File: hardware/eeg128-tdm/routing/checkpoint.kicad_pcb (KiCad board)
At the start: 4 copper layers, 190 x 110 mm, 642 parts, among them J1 J1, J10 J10, J11 J11, J2 J2, J3 J3, J4 J4, J5 J5, J6 J6, J7 J7, J8 J8, J9 TYPE-C-31-M-12, U1 U1, U10 U10, U11 U11, U12 U12, U13 U13, U14 U14, U15 U15, U16 U16, U17 U17, U18 U18, U19 U19, U2 U2, U20 U20, U21 U21, U22 U22, U23 U23, U24 U24, U25 U25, U26 U26, U27 U27, U3 U3, U4 U4, U5 U5, U6 U6, U7 U7, U8 U8, U9 U9, Y1 Y1

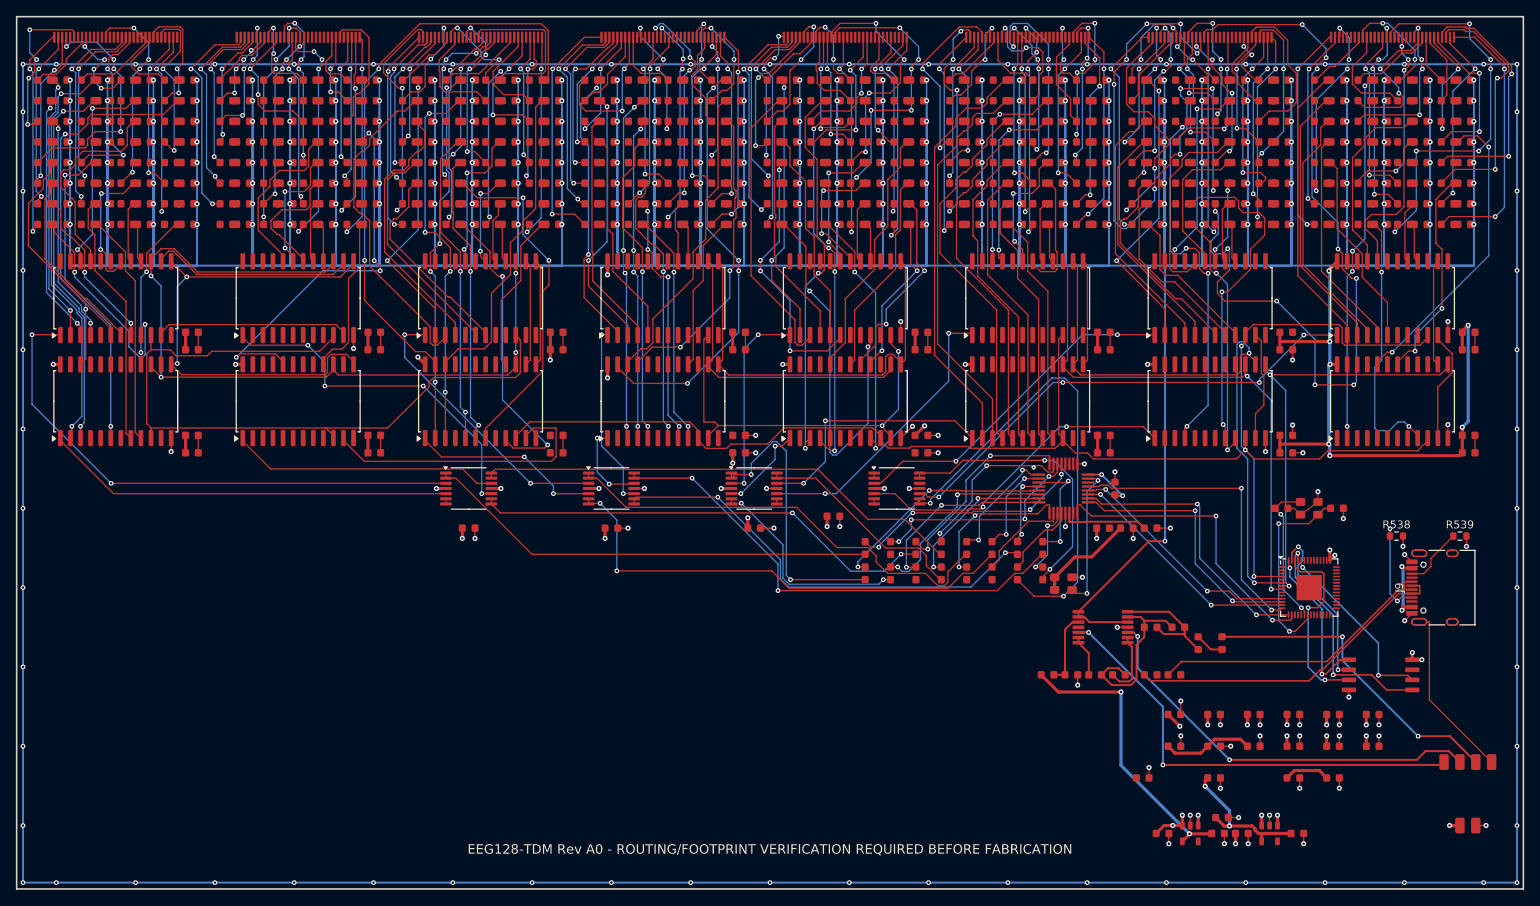
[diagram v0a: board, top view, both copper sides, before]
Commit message: Continue A2 at 316 opens and guard sensitive analog layer routing
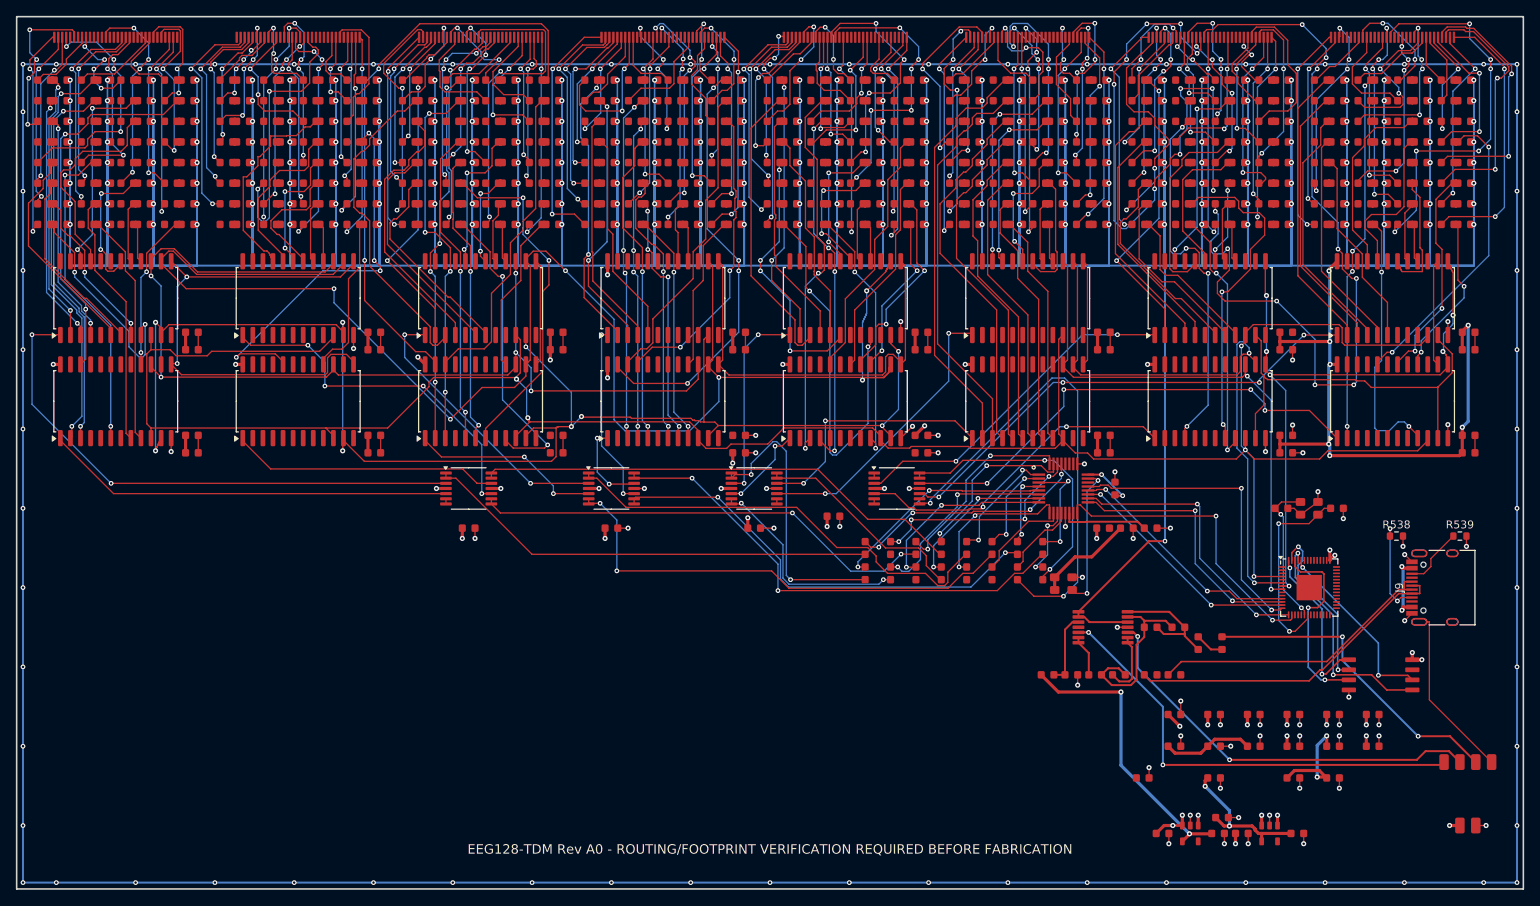
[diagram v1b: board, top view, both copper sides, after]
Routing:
- net MUX_S2: track 168.6 -> 295.6 mm, vias 2 -> 8
- net MUX_S1: track 140.3 -> 235.9 mm, vias 2 -> 9
- net BANK7_N_MUX_OUT: track 0.00 -> 61.8 mm, vias 0 -> 4
- net CH018_N_ELECTRODE: track 0.00 -> 34.9 mm, vias 0 -> 2
- net MUX_EN: track 171.4 -> 200.6 mm, vias 6 -> 7
- net MUX_S3: track 197.1 -> 224.3 mm, vias 4 -> 8
- net CH026_P_MUX: track 0.50 -> 26.4 mm
- net CH127_N_MUX: track 0.50 -> 20.9 mm, vias 0 -> 2
- net CH125_P_MUX: track 0.50 -> 16.4 mm
- net CH054_N_ELECTRODE: track 0.00 -> 13.3 mm
- net 3V3D: track 53.9 -> 60.9 mm, vias 15 -> 16
- net MUX_S0: track 295.6 -> 302.0 mm, vias 3 -> 5

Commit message: Resume validated A2 routing from 313 native opens
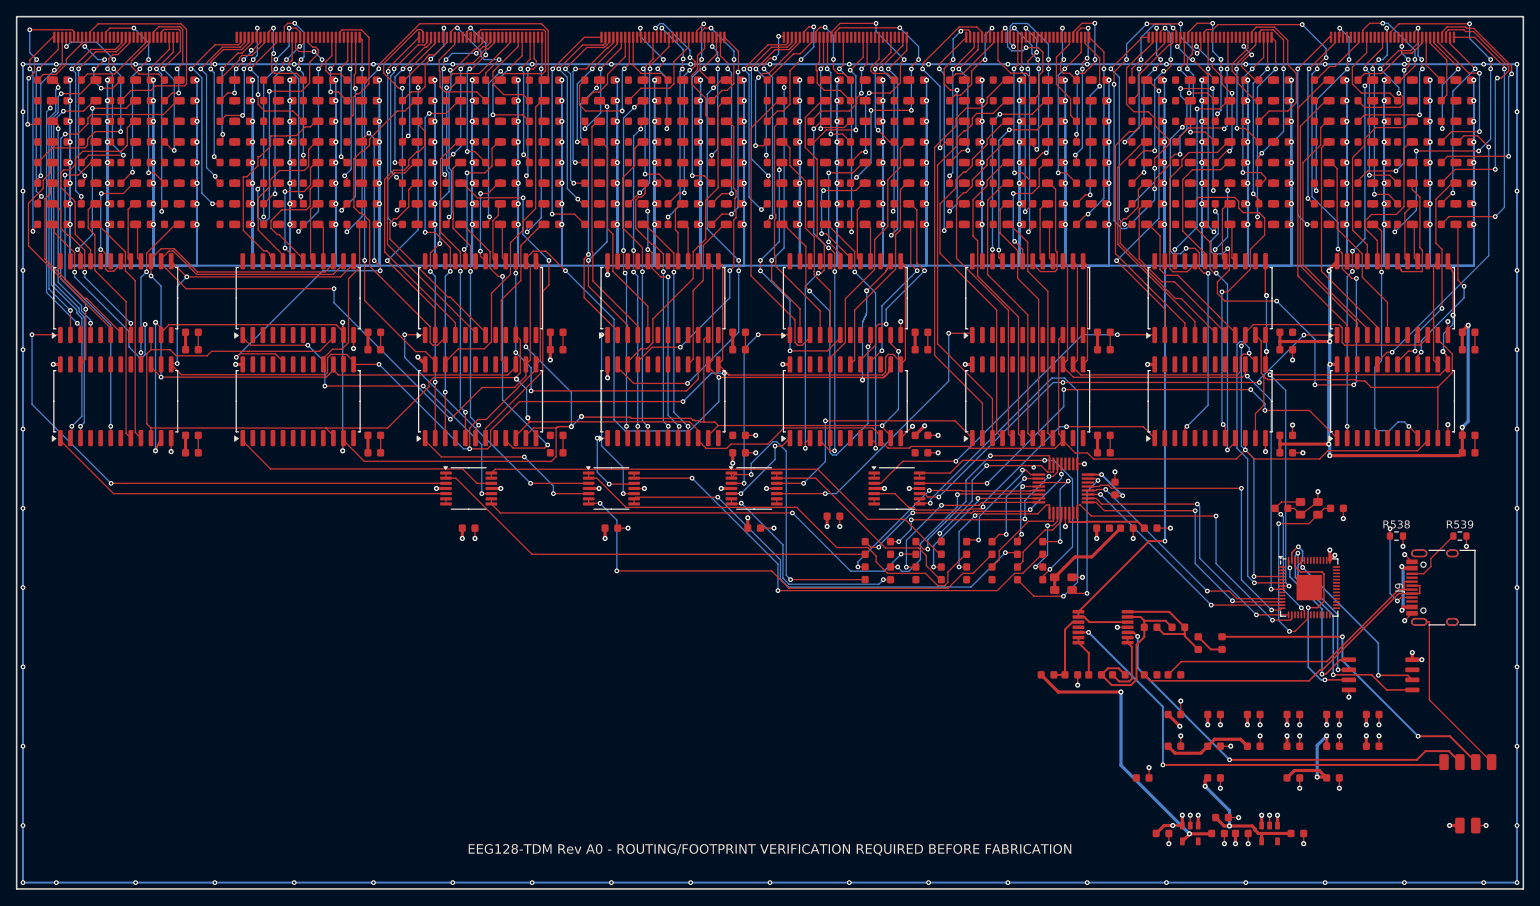
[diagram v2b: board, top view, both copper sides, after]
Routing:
- net MUX_S3: track 224.3 -> 296.0 mm, vias 8 -> 12
- net CH009_P_ELECTRODE: track 0.00 -> 29.6 mm

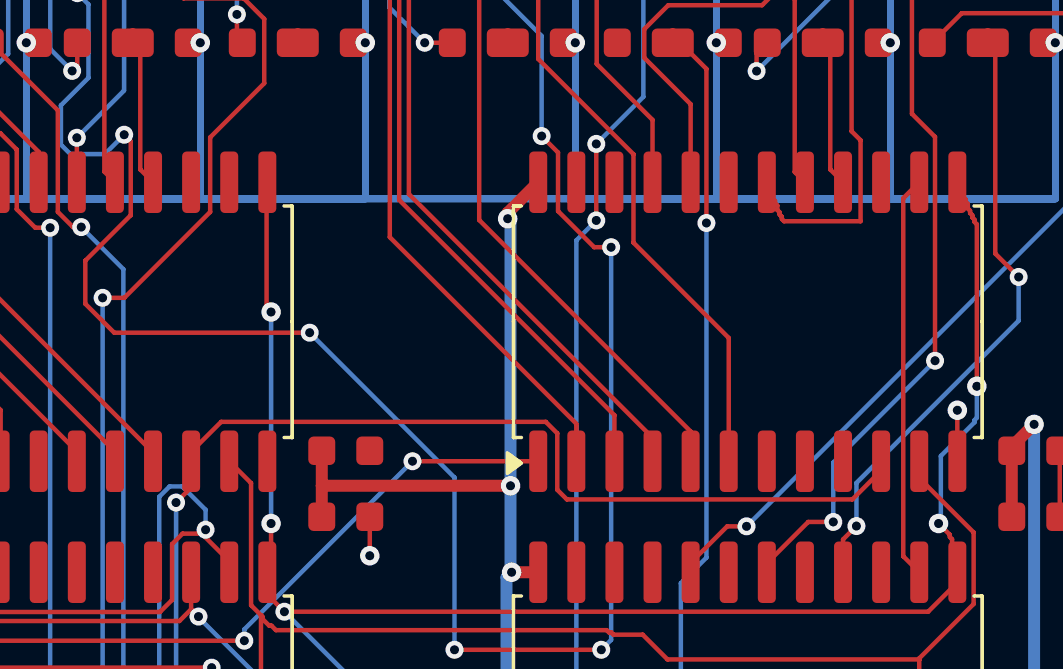
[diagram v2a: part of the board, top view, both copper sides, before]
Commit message: Save native-clean A2 checkpoint at 312 opens
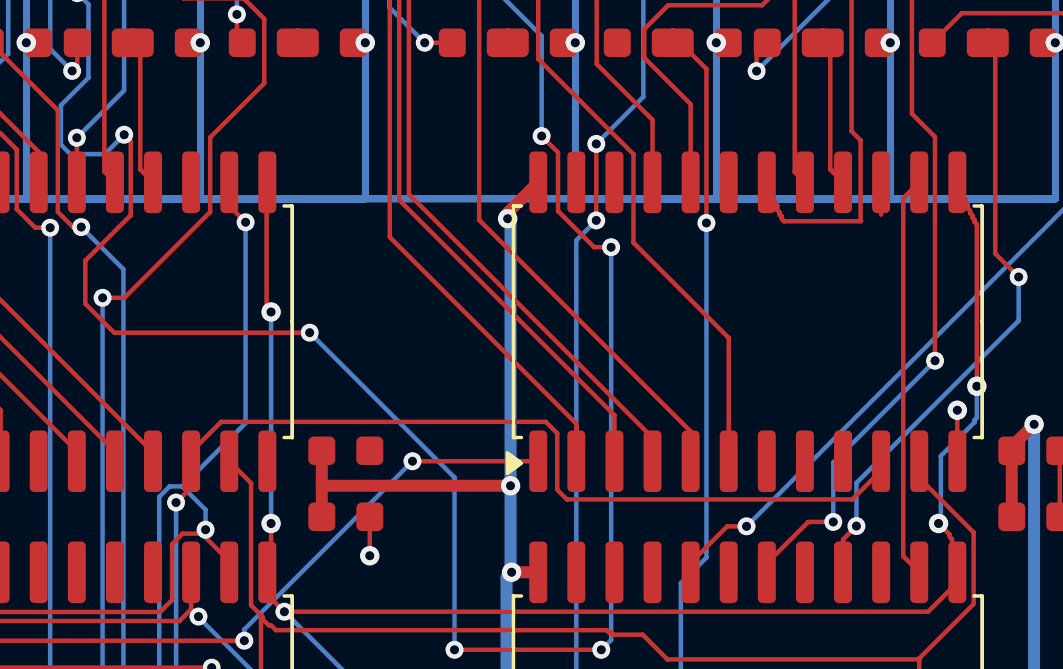
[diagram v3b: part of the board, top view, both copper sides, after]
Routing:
- net MUX_S2: track 295.6 -> 306.9 mm, vias 8 -> 9
- net MUX_EN: track 200.6 -> 201.7 mm

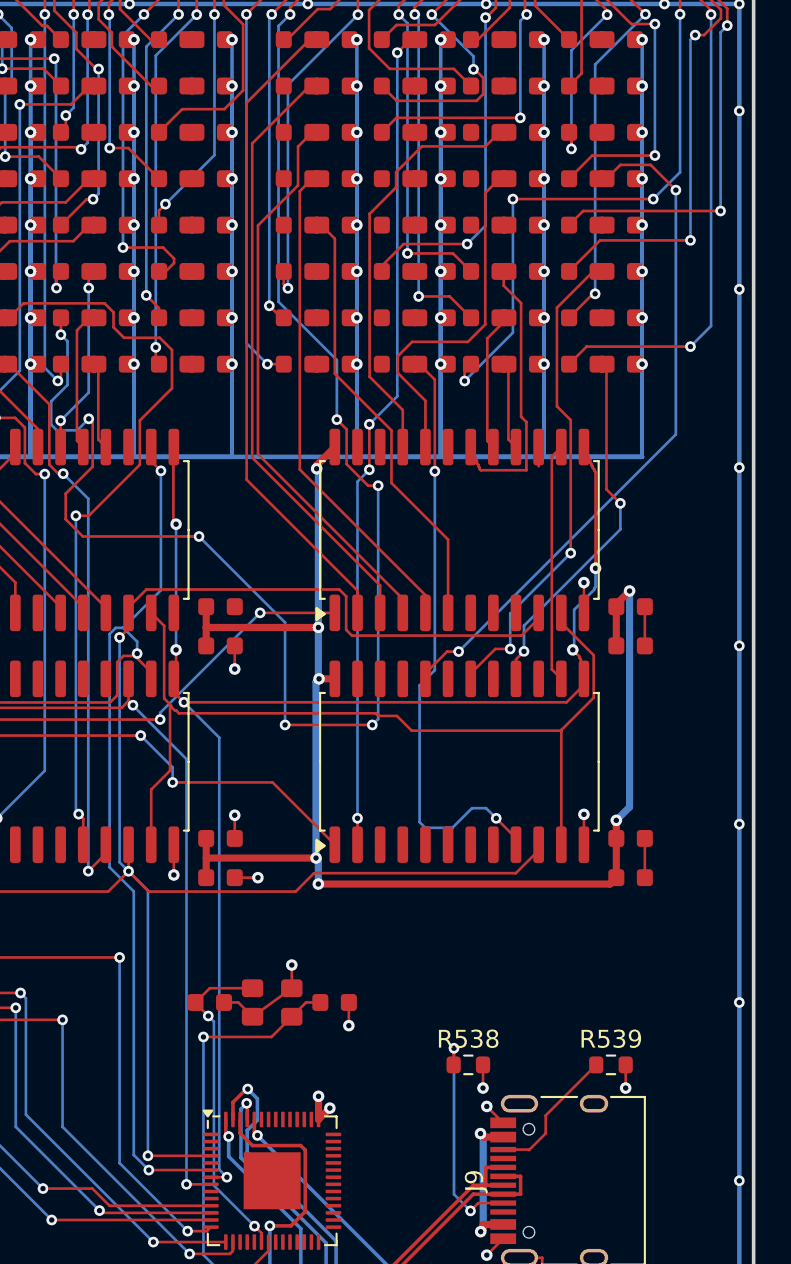
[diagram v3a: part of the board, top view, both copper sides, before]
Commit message: Continue validated A2 checkpoint at 310 native opens
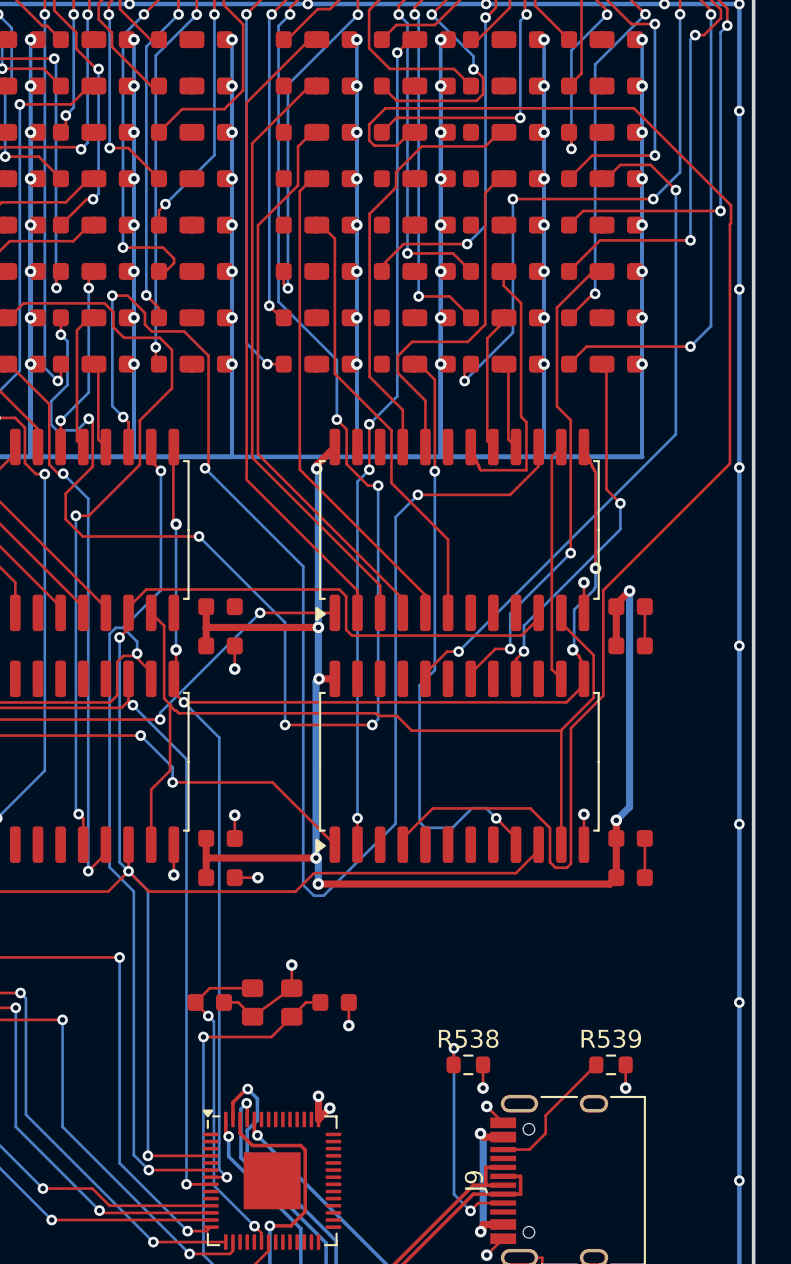
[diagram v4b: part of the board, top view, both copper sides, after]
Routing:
- net MUX_EN: track 201.7 -> 283.3 mm, vias 7 -> 11
- net CH117_N_MUX: track 0.50 -> 80.8 mm
